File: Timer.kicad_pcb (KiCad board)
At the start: 2 copper layers, 64 x 100 mm, 36 parts, among them J1 Conn_01x04, SW1 SW_Push, SW10 SW_Push, SW11 SW_Push, SW12 SW_Push, SW2 SW_Push, SW3 SW_Push, SW4 SW_Push, SW5 SW_Push, SW6 SW_Push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

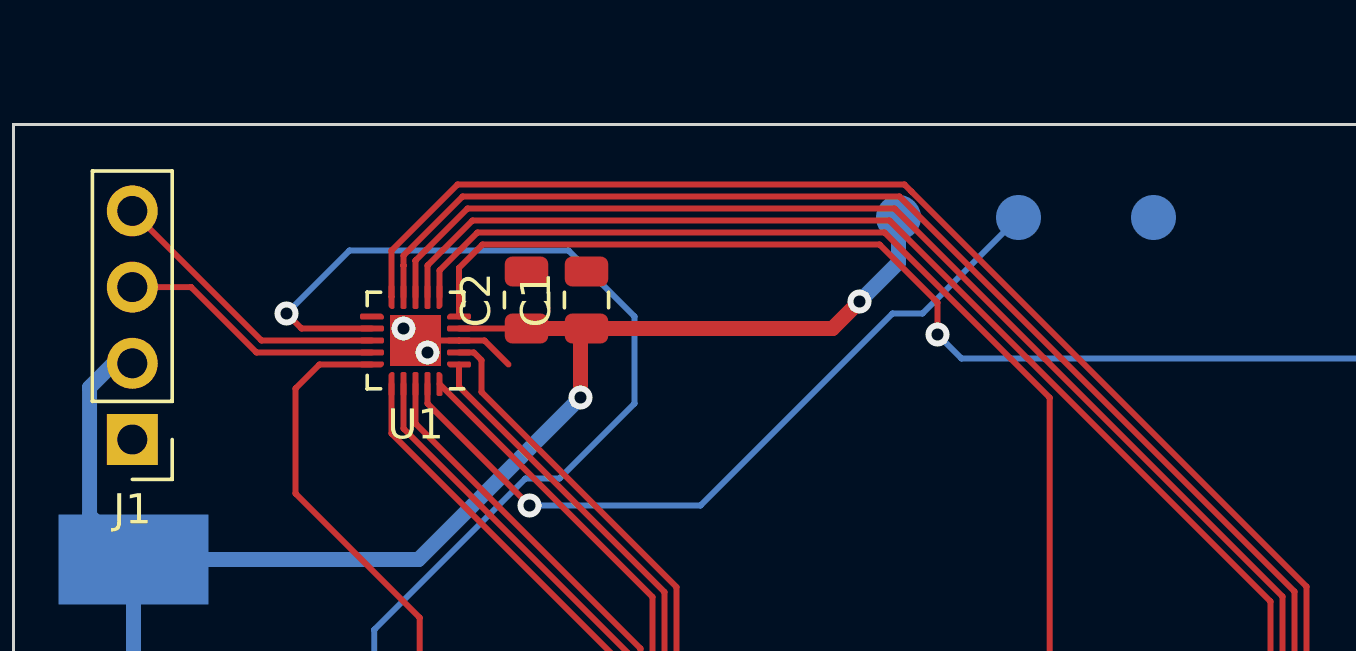
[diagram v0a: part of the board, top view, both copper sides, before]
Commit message: add Silkscreen move Testpoints
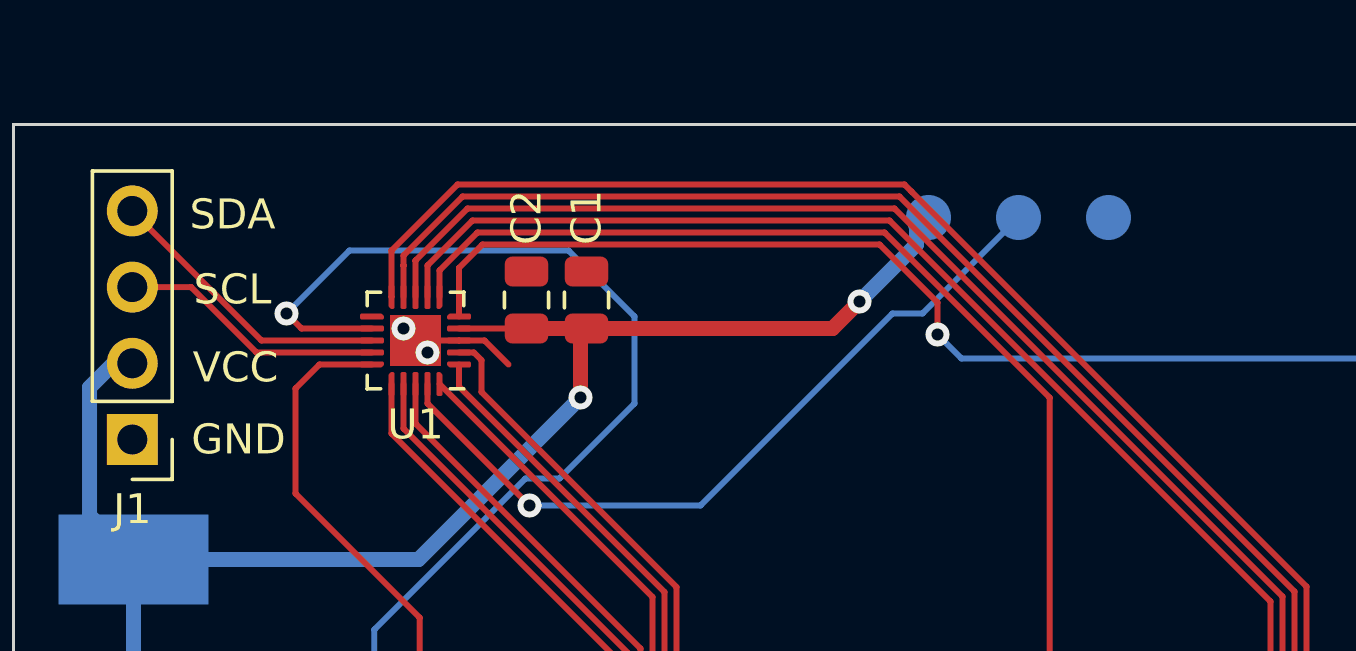
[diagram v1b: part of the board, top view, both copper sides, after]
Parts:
- moved TP3 1.50 mm to (129.5, 30.1)
- moved TP1 1.00 mm to (123.5, 30.1)
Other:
- board text added: "GND"
- board text added: "SCL"
- board text added: "SDA"
- board text added: "UDPI"
- board text added: "VCC"
